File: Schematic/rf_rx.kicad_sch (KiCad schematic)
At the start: 12 parts, among them SW2 TS24CA, U1 ME6217C33M5G, U12 ESP-01F-2M, U13 E28-2G4M27SX

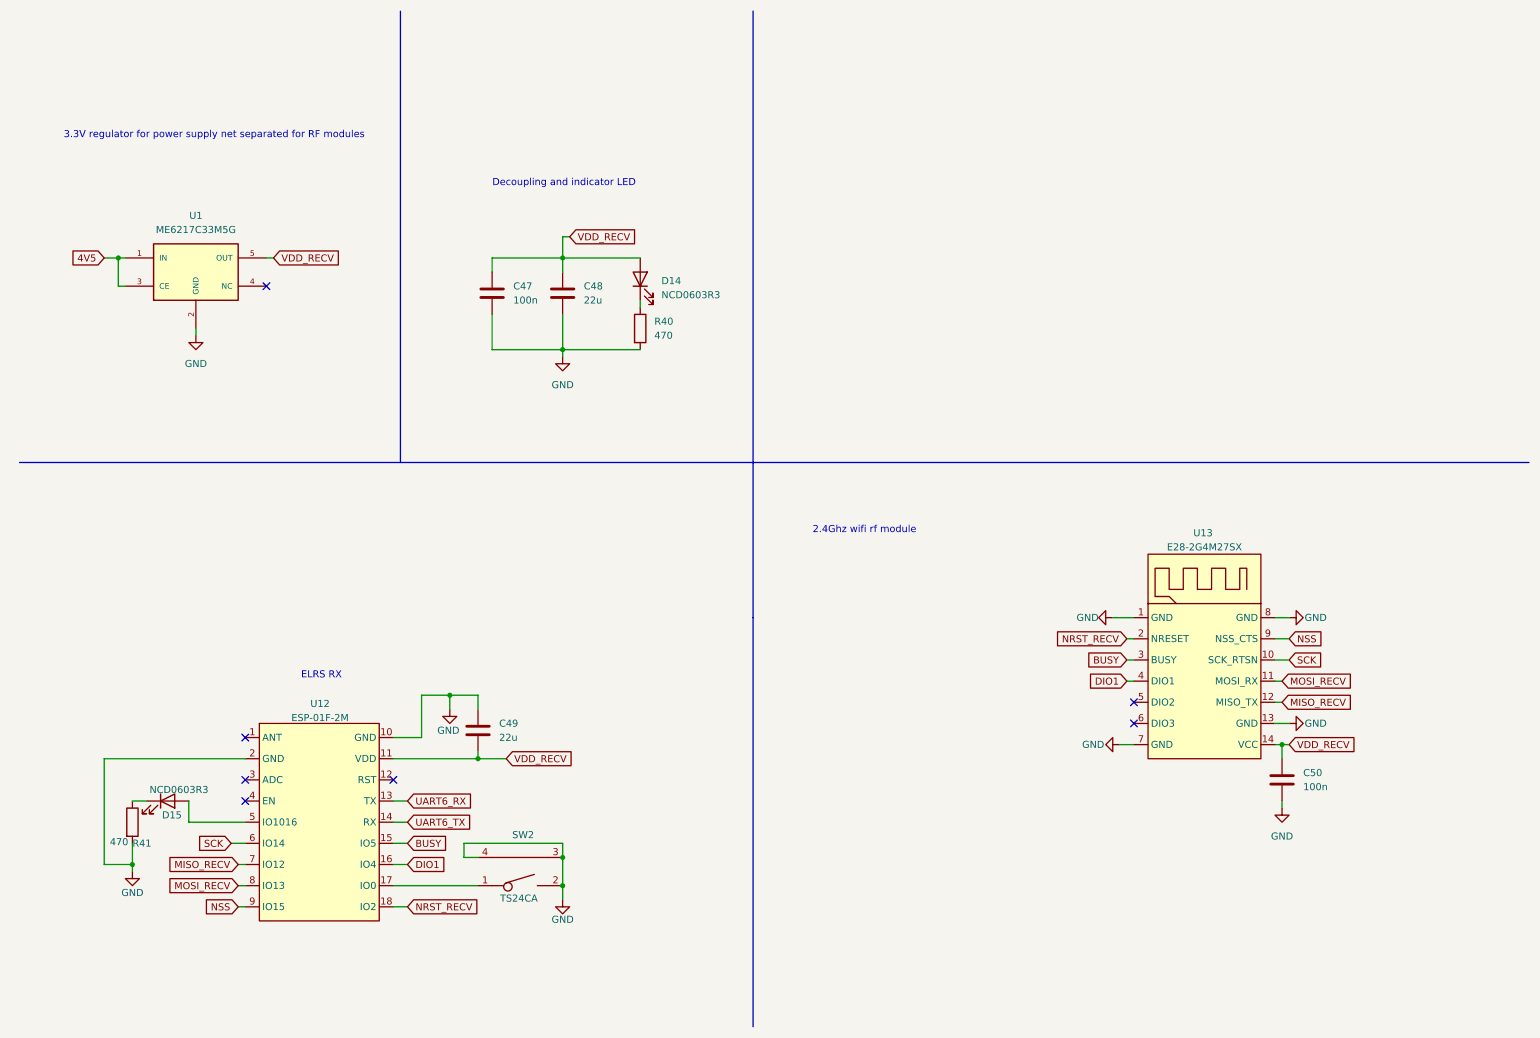
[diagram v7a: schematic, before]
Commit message: refactor : improve readability and portability of the project
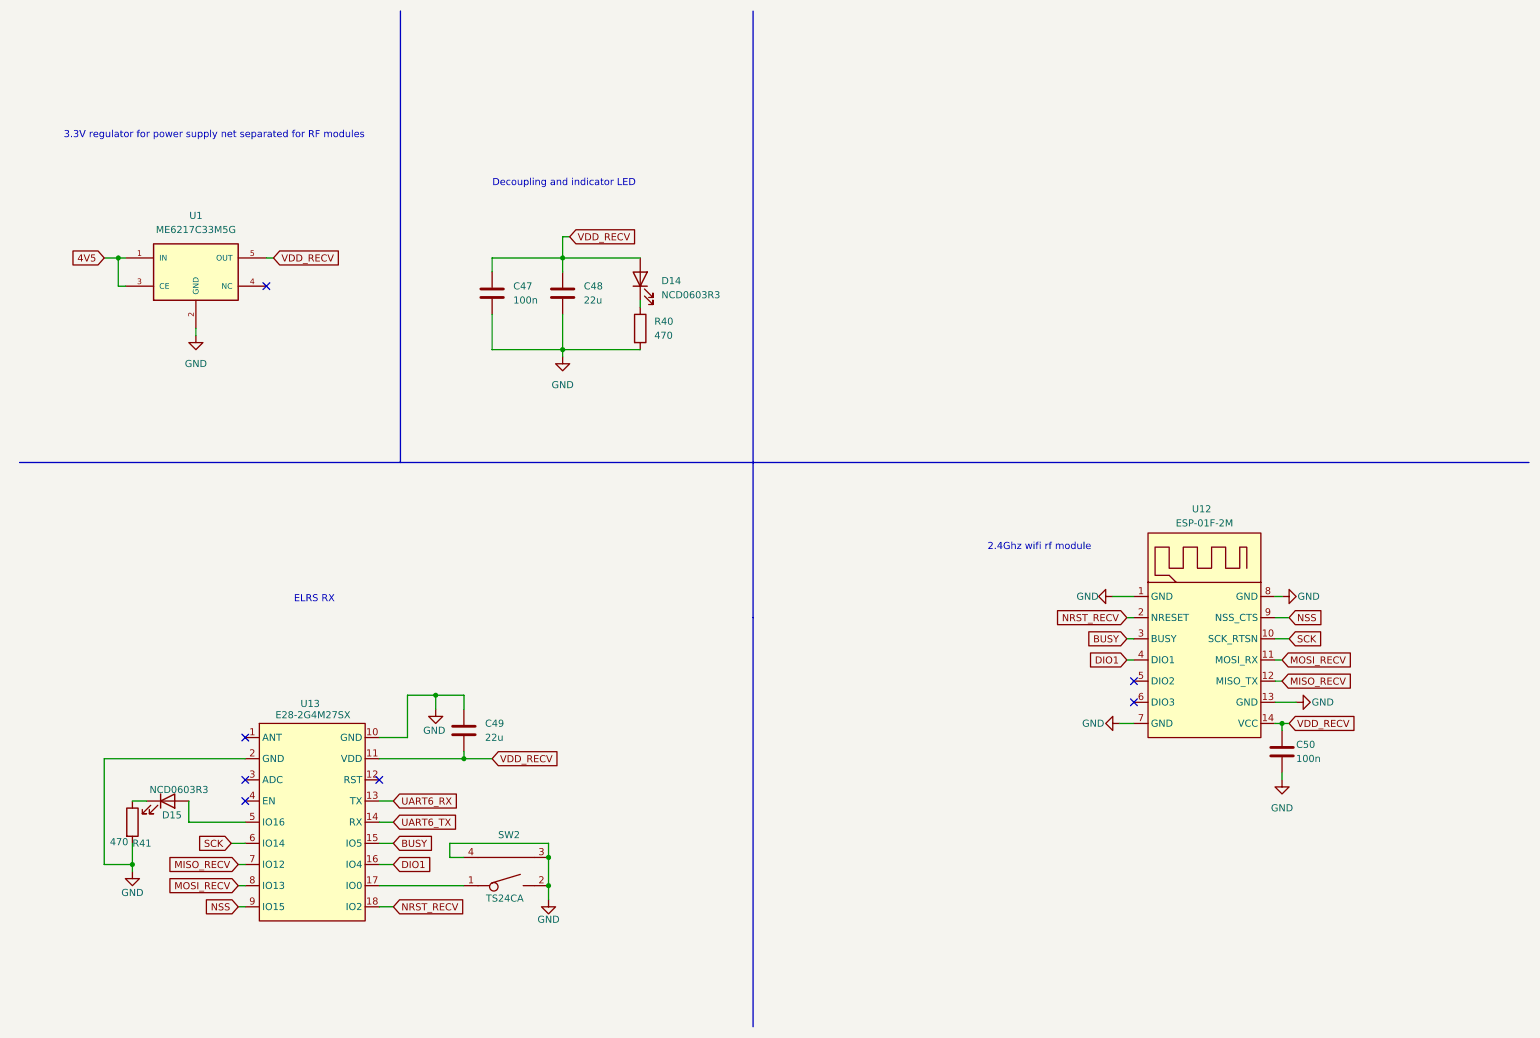
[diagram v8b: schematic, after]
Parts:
- U12: footprint fch7_fp:WIFIM-SMD_ESP-01F-2M -> fch7_fp:WIRELM-SMD_E28-2G4M27SX; symbol fclib:elrs_rx -> fclib:RF_2.4
- U13: footprint fch7_fp:WIRELM-SMD_E28-2G4M27SX -> fch7_fp:WIFIM-SMD_ESP-01F-2M; symbol fclib:RF_2.4 -> fclib:elrs_rx; Fréquence (none) -> 2.4G
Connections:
- net BUSY: now also U12.3 (BUSY), U13.15 (IO5); no longer U12.15 (IO5), U13.3 (BUSY)
- net DIO1: now also U12.4 (DIO1), U13.16 (IO4); no longer U12.16 (IO4), U13.4 (DIO1)
- net GND: now also U12.1 (GND), U12.13 (GND), U12.7 (GND), U12.8 (GND), U13.10 (GND), U13.2 (GND); no longer U12.10 (GND), U12.2 (GND), U13.1 (GND), U13.13 (GND), U13.7 (GND), U13.8 (GND)
- net MISO_RECV: now also U12.12 (MISO_TX), U13.7 (IO12); no longer U12.7 (IO12), U13.12 (MISO_TX)
- net MOSI_RECV: now also U12.11 (MOSI_RX), U13.8 (IO13); no longer U12.8 (IO13), U13.11 (MOSI_RX)
- net NRST_RECV: now also U12.2 (NRESET), U13.18 (IO2); no longer U12.18 (IO2), U13.2 (NRESET)
- net SCK: now also U12.10 (SCK_RTSN), U13.6 (IO14); no longer U12.6 (IO14), U13.10 (SCK_RTSN)
- net UART6_RX: now also U13.13 (TX); no longer U12.13 (TX)
- net UART6_TX: now also U13.14 (RX); no longer U12.14 (RX)
- net VDD_RECV: now also U12.14 (VCC), U13.11 (VDD); no longer U12.11 (VDD), U13.14 (VCC)
- net at D15.2 (A): now also U13.5 (IO16); no longer U12.5 (IO1016)
- net at SW2.1: now also U13.17 (IO0); no longer U12.17 (IO0)
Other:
- moved on the sheet: C49, C50, SW2
